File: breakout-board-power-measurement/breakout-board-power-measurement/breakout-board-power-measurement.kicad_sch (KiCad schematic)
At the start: 62 parts, among them J1 Screw_Terminal_01x04, J2 Conn_01x07, J3 Conn_01x07, J4 Conn_01x02, Q1 NMOS, Q2 NMOS, U1 MCP3911A0-E/SS, U2 Si8641BA-B-IU, U3 LM317_3PinPackage, U4 LM2575-3.3BT, Y1 10M

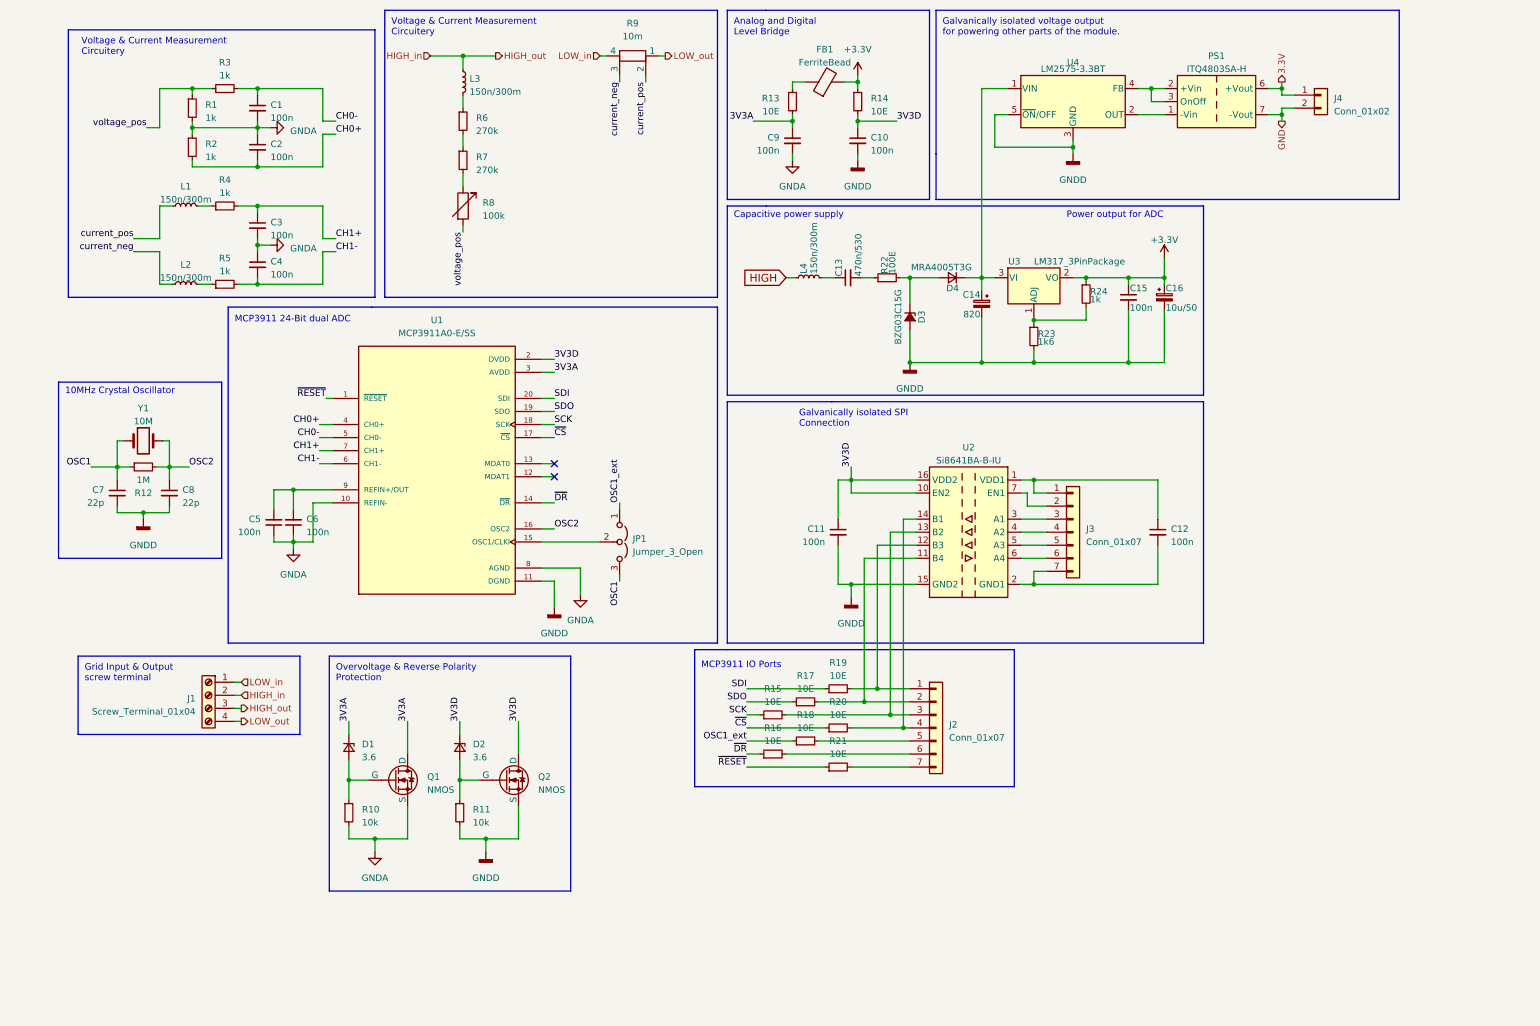
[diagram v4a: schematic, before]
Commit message: Added MCP3911 lib to project specific libraries
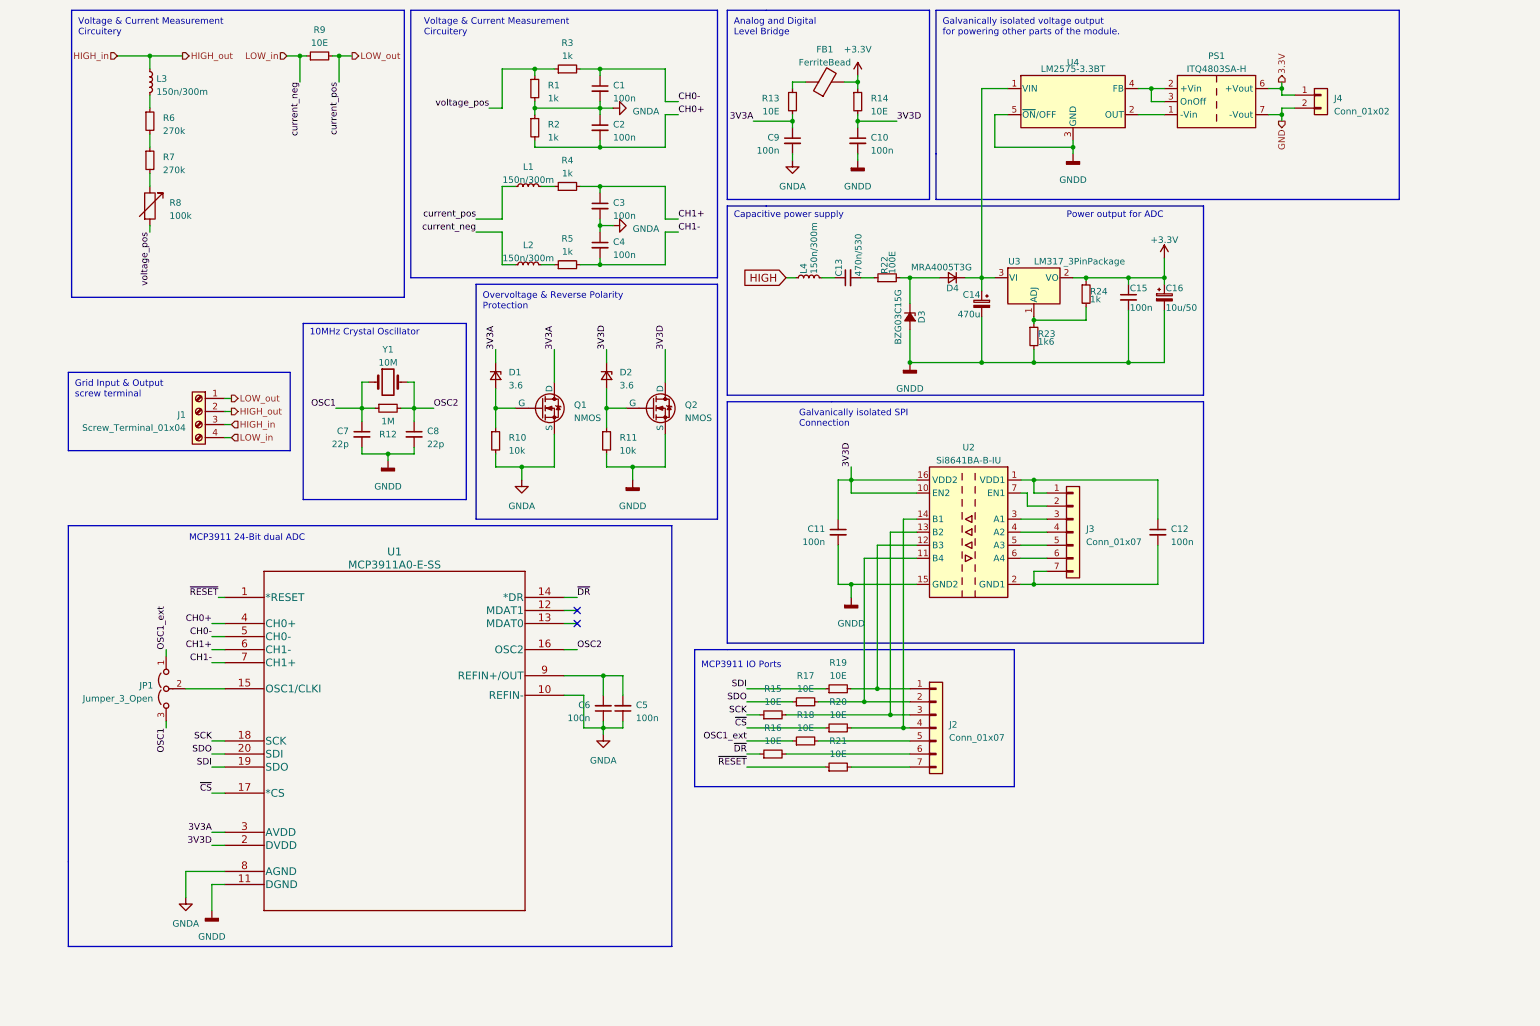
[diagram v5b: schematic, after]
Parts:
- removed R9: 10m, Resistors_THT:R_Axial_DIN0516_L15.5mm_D5.0mm_P20.32mm_Horizontal, symbol Device:R_Shunt
- removed U1: MCP3911A0-E/SS, Housings_SSOP:SSOP-20_5.3x7.2mm_Pitch0.65mm, symbol MCP3911A0-E_SS:MCP3911A0-E/SS
- added R9: 10E, Resistor_SMD:R_2816_7142Metric, symbol Device:R_Small
- added U1: MCP3911A0-E-SS, MCP3911A0-E-SS:MCP3911A0-E&slash_SS, symbol 2023-03-06_20-07-43:MCP3911A0-E/SS
- C13: footprint Capacitors_THT:C_Rect_L26.5mm_W10.5mm_P22.50mm_MKS4 -> Capacitor_THT:C_Rect_L26.5mm_W10.5mm_P22.50mm_MKS4
- C14: value 820 -> 470u; footprint Capacitors_Tantalum_SMD:CP_Tantalum_Case-D_EIA-7343-31_Hand -> Capacitor_Tantalum_SMD:CP_EIA-7343-31_Kemet-D_Pad2.25x2.55mm_HandSolder
- C15: footprint Capacitors_SMD:C_1206_HandSoldering -> Capacitor_SMD:C_1206_3216Metric_Pad1.33x1.80mm_HandSolder
- C16: footprint Capacitors_Tantalum_SMD:CP_Tantalum_Case-D_EIA-7343-31_Hand -> Capacitor_Tantalum_SMD:CP_EIA-7343-31_Kemet-D_Pad2.25x2.55mm_HandSolder
- D1, D2: footprint (none) -> Diode_SMD:D_1206_3216Metric
- D3, D4: footprint Diodes_SMD:D_SMA-SMB_Universal_Handsoldering -> Diode_SMD:D_SMA-SMB_Universal_Handsoldering
- FB1: footprint (none) -> Diode_SMD:D_SMA-SMB_Universal_Handsoldering
- J1: footprint (none) -> TerminalBlock:TerminalBlock_Altech_AK300-4_P5.00mm
- JP1: footprint Pin_Headers:Pin_Header_Straight_1x03_Pitch2.54mm -> Connector_PinHeader_2.54mm:PinHeader_1x03_P2.54mm_Vertical
- L1, L2, L3, L4: footprint Inductors_SMD:L_1206_HandSoldering -> Inductor_SMD:L_1206_3216Metric_Pad1.22x1.90mm_HandSolder
- Q1, Q2: footprint (none) -> Package_TO_SOT_SMD:TO-252-2
- R22, R23, R24: footprint Resistors_SMD:R_1206_HandSoldering -> Resistor_SMD:R_1206_3216Metric_Pad1.30x1.75mm_HandSolder
- R8: footprint Resistor_SMD:R_1206_3216Metric_Pad1.30x1.75mm_HandSolder -> Potentiometer_THT:Potentiometer_ACP_CA9-V10_Vertical_Hole
- U3: footprint TO_SOT_Packages_SMD:SOT-89-3_Handsoldering -> Package_TO_SOT_SMD:SOT-89-3_Handsoldering
- Y1: footprint Crystals:Crystal_HC49-4H_Vertical -> Crystal:Crystal_HC49-4H_Vertical
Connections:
- net current_neg is gone; now on net LOW_in: L2.1
- net current_pos is gone; now on net LOW_out: L1.1
- net 3V3A: now also U1.3 (AVDD)
- net 3V3D: now also U1.2 (DVDD)
- net CH0+: now also U1.4 (CH0+)
- net CH0-: now also U1.5 (CH0-)
- net CH1+: now also U1.6 (CH1-)
- net CH1-: now also U1.7 (CH1+)
- net GNDA: now also U1.10 (REFIN-), U1.8 (AGND)
- net GNDD: now also U1.11 (DGND)
- net LOW_in: now also J1.4 (Pin_4), R9.1; no longer J1.1 (Pin_1)
- net LOW_out: now also J1.1 (Pin_1), R9.2; no longer J1.4 (Pin_4)
- net OSC2: now also U1.16 (OSC2)
- net SCK: now also U1.18 (SCK)
- net SDI: now also U1.19 (SDO)
- net SDO: now also U1.20 (SDI)
- net ~{CS}: now also U1.17 (*CS)
- net ~{DR}: now also U1.14 (*DR)
- net ~{RESET}: now also U1.1 (*RESET)
- net at C5.2, C6.2: now also U1.9 (REFIN+/OUT)
- net at JP1.2 (C): now also U1.15 (OSC1/CLKI)
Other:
- moved on the sheet: C1, C2, C3, C4, C5, C6, C7, C8, D1, D2, J1, JP1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

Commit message: Important updates and fine tunings to schematic
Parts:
- removed D1, D2: 3.6, Diode_SMD:D_1206_3216Metric, symbol Device:D_Zener_Small
- removed PS1: ITQ4803SA-H, Converter_DCDC:Converter_DCDC_XP_POWER-ITQxxxxS-H_THT, symbol Converter_DCDC:ITQ4803SA-H
- removed Q1, Q2: NMOS, Package_TO_SOT_SMD:TO-252-2, symbol Simulation_SPICE:NMOS
- removed U3: LM317_3PinPackage, Package_TO_SOT_SMD:SOT-89-3_Handsoldering, symbol Power-Analyzer-rescue:LM317_3PinPackage
- removed U4: LM2575-3.3BT, Package_TO_SOT_THT:TO-220-5_Vertical, symbol Regulator_Switching:LM2575-3.3BT
- added PS2: IA0505S, Converter_DCDC:Converter_DCDC_XP_POWER-IAxxxxS_THT, symbol Converter_DCDC:IA0505S
- added U3: LM317_TO-252, Package_TO_SOT_SMD:TO-252-2, symbol Regulator_Linear:LM317_TO-252
- J2: value Conn_01x07 -> Conn_01x09; footprint Connector_PinSocket_2.54mm:PinSocket_1x07_P2.54mm_Vertical -> Connector_PinSocket_2.54mm:PinSocket_1x09_P2.54mm_Vertical; symbol Connector_Generic:Conn_01x07 -> Connector_Generic:Conn_01x09
- R10, R11: value 10k -> 180k
- R6, R7: value 270k -> 150k
- R8: value 100k -> 10k
- R9: value 10E -> 50m
- U2: footprint Package_SO:QSOP-16_3.9x4.9mm_P0.635mm -> Package_SO:SOIC-16_3.9x9.9mm_P1.27mm
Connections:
- net +3V3: now also U3.2 (VO)
- net 3.3V: now also PS2.1 (+Vin)
- net 3V3D: now also J2.8 (Pin_8)
- net GND: now also PS2.2 (-Vin)
- net GNDA: no longer R10.2
- net GNDD: now also J2.9 (Pin_9), PS2.4 (-Vout), PS2.5 (0V); no longer R11.2
- net at R10.1: now also R7.2
- net at R11.1: now also R10.2
- net at R8.1: now also R11.2; no longer R7.2
- net at R23.1, R24.2: now also U3.1 (ADJ)
- net at C14.1, D4.1 (K): now also PS2.6 (+Vout), U3.3 (VI)
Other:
- note removed: "Overvoltage & Reverse Polarity Protection"
- moved on the sheet: C1, C10, C11, C12, C13, C14, C15, C16, C2, C3, C4, C5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

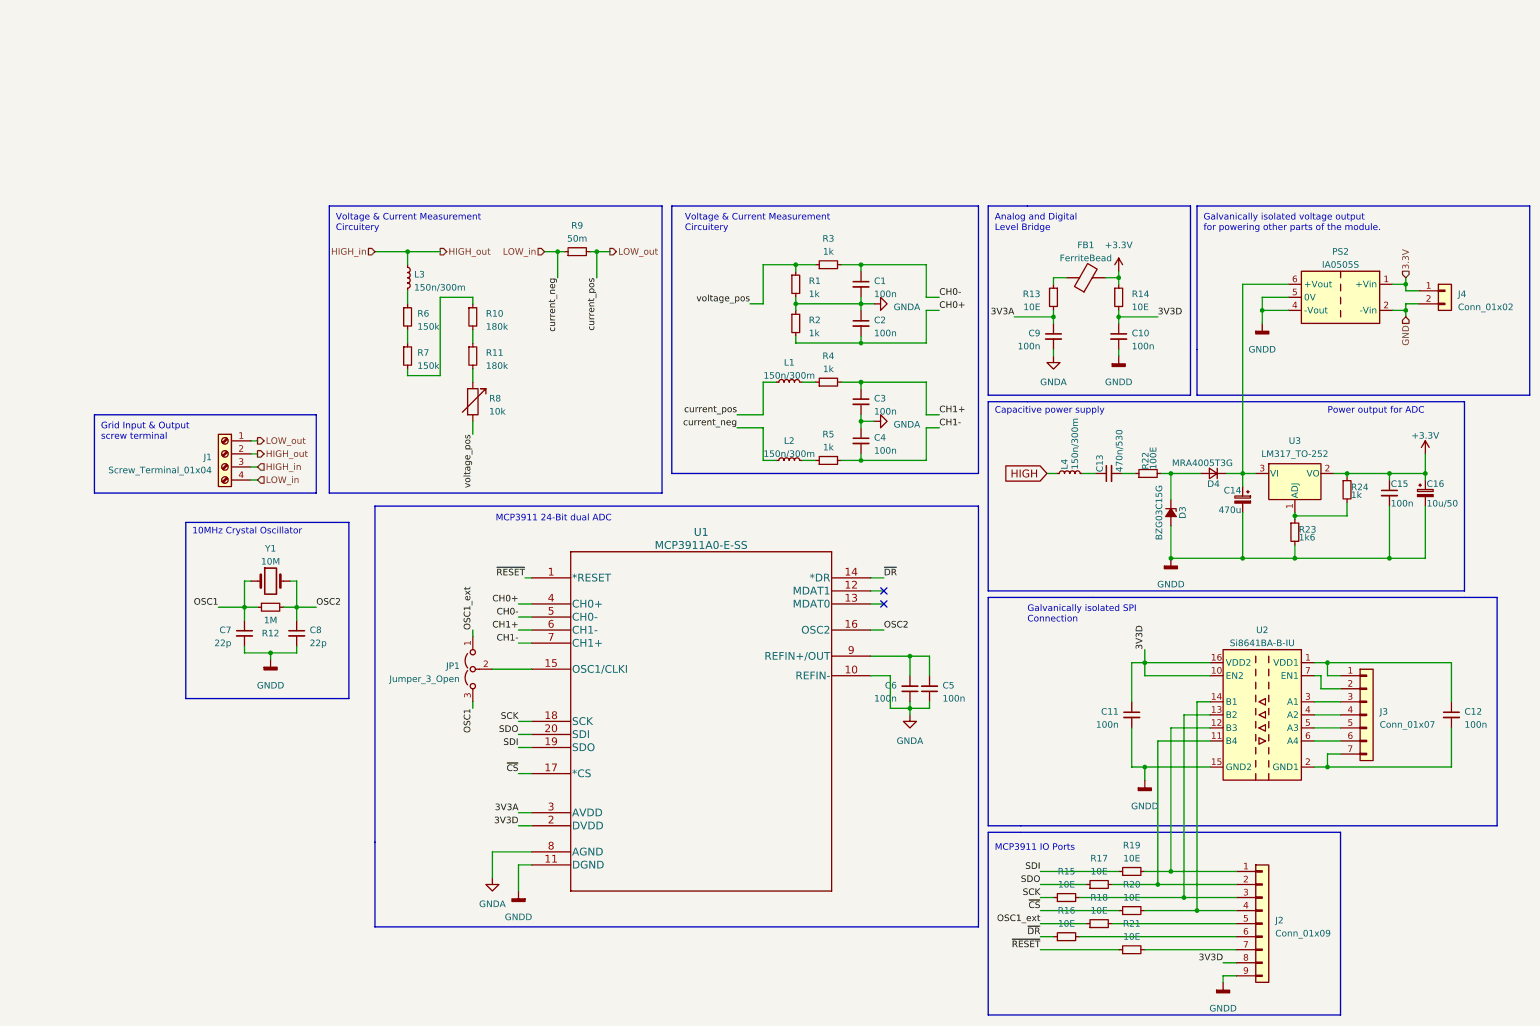
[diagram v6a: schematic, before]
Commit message: Power measurement PCB 95% Done. Whats missing: proper cooil footprints, capacitive power supply net
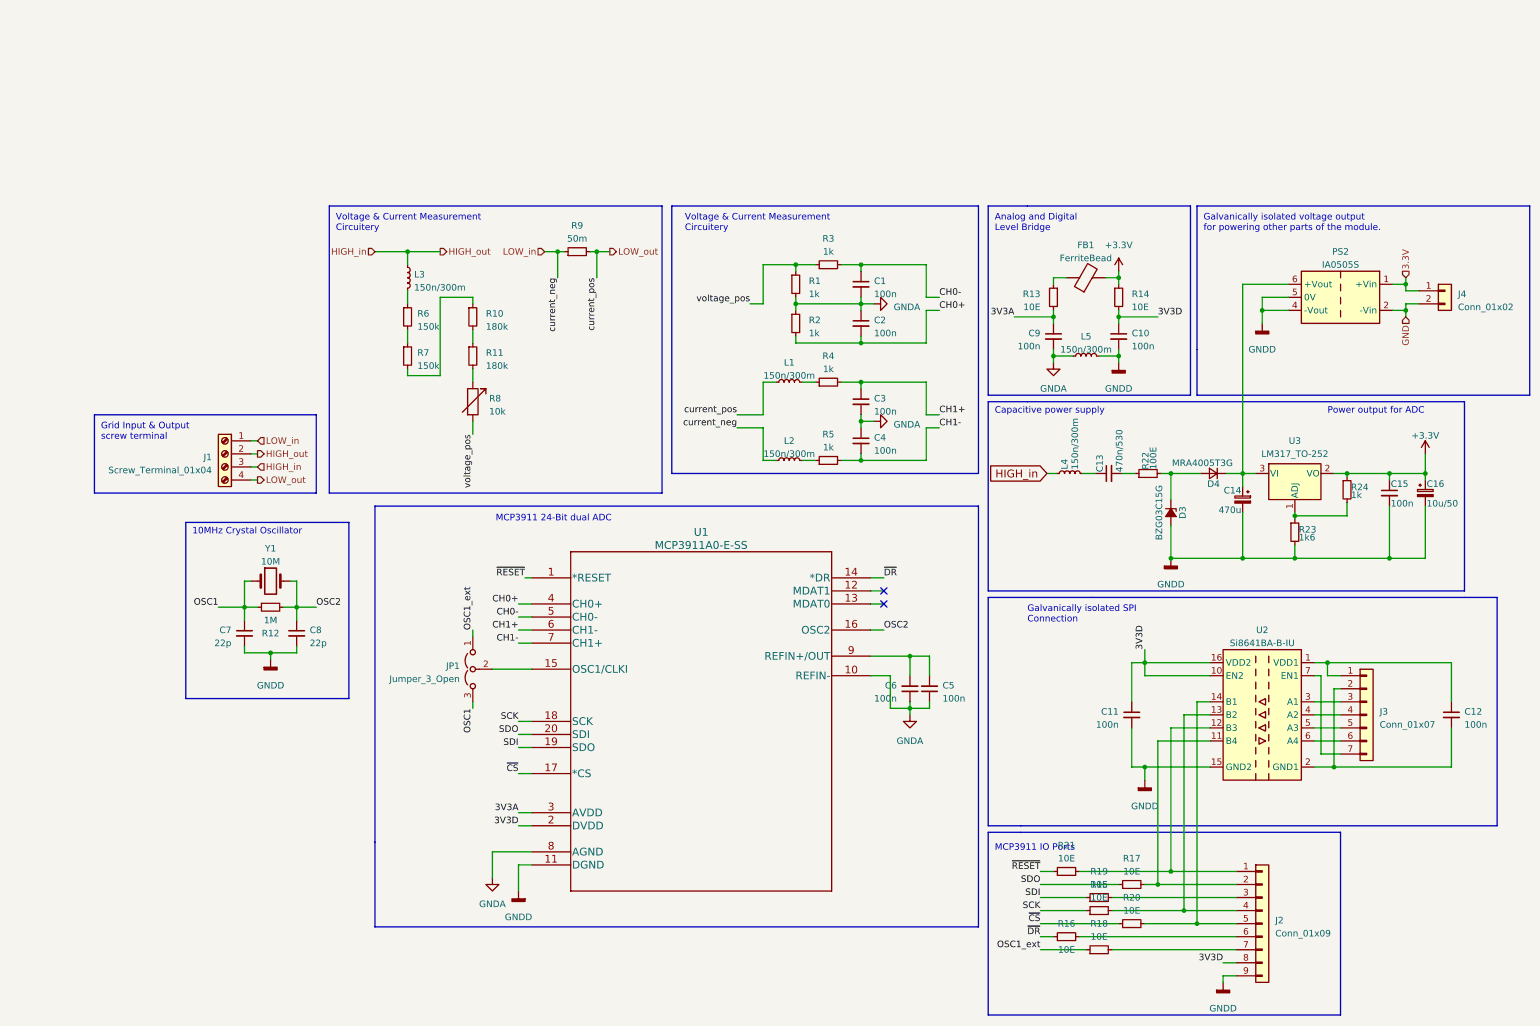
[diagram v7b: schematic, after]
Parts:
- added L5: 150n/300m, Inductor_SMD:L_7.3x7.3_H4.5, symbol Device:L_Small
- L1, L2, L3, L4: footprint Inductor_SMD:L_1206_3216Metric_Pad1.22x1.90mm_HandSolder -> Inductor_SMD:L_7.3x7.3_H4.5
- R9: footprint Resistor_SMD:R_2816_7142Metric -> Resistor_THT:R_Axial_DIN0516_L15.5mm_D5.0mm_P20.32mm_Horizontal
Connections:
- net HIGH is gone; now on net HIGH_in: L4.1
- net GNDA: now also L5.1
- net GNDD: now also L5.2
- net LOW_in: now also J1.1 (Pin_1); no longer J1.4 (Pin_4)
- net LOW_out: now also J1.4 (Pin_4); no longer J1.1 (Pin_1)
- net at J3.2 (Pin_2): now also C12.2, U2.2 (GND1), U2.8 (GND1); no longer U2.7 (EN1)
- net at J2.1 (Pin_1), U2.12 (B3): now also R21.2; no longer R19.2
- net at R15.2, U2.13 (B2): now also J2.4 (Pin_4); no longer J2.3 (Pin_3)
- net at R20.2, U2.14 (B1): now also J2.5 (Pin_5); no longer J2.4 (Pin_4)
- net at R18.2: now also J2.7 (Pin_7); no longer J2.5 (Pin_5)
- new net: J3.7 (Pin_7), U2.7 (EN1)
- new net: J2.3 (Pin_3), R19.2
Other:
- moved on the sheet: R15, R17, R18, R19, R20

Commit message: Breakout Board: Power Measurement - status: done.. yaygit add -A!
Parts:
- added R10, R11, R7, R8: 10m, Resistor_SMD:R_1210_3225Metric, symbol Device:R_Small
- J2: footprint Connector_PinSocket_2.54mm:PinSocket_1x09_P2.54mm_Vertical -> Connector_PinHeader_2.54mm:PinHeader_1x09_P2.54mm_Vertical
- J3: footprint Connector_PinSocket_2.54mm:PinSocket_1x07_P2.54mm_Vertical -> Connector_PinHeader_2.54mm:PinHeader_1x07_P2.54mm_Vertical
- J4: footprint Connector_PinSocket_2.54mm:PinSocket_1x02_P2.54mm_Vertical -> Connector_PinHeader_2.54mm:PinHeader_1x02_P2.54mm_Vertical
- L1: renamed from L3; footprint Inductor_SMD:L_7.3x7.3_H4.5 -> Inductor_SMD:L_1206_3216Metric
- L2: renamed from L1; footprint Inductor_SMD:L_7.3x7.3_H4.5 -> Inductor_SMD:L_1206_3216Metric
- L3: renamed from L2; footprint Inductor_SMD:L_7.3x7.3_H4.5 -> Inductor_SMD:L_1206_3216Metric
- L4, L5: footprint Inductor_SMD:L_7.3x7.3_H4.5 -> Inductor_SMD:L_1206_3216Metric
- R4: renamed from R9; value 50m -> 10m; footprint Resistor_THT:R_Axial_DIN0516_L15.5mm_D5.0mm_P20.32mm_Horizontal -> Resistor_SMD:R_1210_3225Metric
- renumbered C7 to C1, C13 to C10, C10 to C11, C11 to C12, C14 to C13, C15 to C14, C16 to C15, C12 to C16, C8 to C2, C1 to C3, C2 to C4, C3 to C5, C4 to C6, C6 to C7, C5 to C8, D3 to D1, D4 to D2, PS2 to PS1, R12 to R1, R1 to R12, R2 to R13, R3 to R14, R4 to R15, R5 to R16, R13 to R17, R21 to R18, R16 to R19, R6 to R2, R19 to R20, R15 to R21, R18 to R22, R14 to R23, R17 to R24, R20 to R25, R22 to R26, R23 to R27, R24 to R28, R7 to R3, R10 to R5, R11 to R6, R8 to R9
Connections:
- net +3V3 is gone; now on net +3.3V: C14.1, C15.1, R28.1, U3.2 (VO)
- net GNDD: no longer PS1.4 (-Vout)
- net LOW_out: now also R11.2; no longer R4.2
- net 3.3V: no longer names the net of J4.1 (Pin_1), PS1.1 (+Vin)
- net GND: no longer names the net of J4.2 (Pin_2), PS1.2 (-Vin)
- new net: R10.2, R11.1
- new net: R10.1, R8.2
- new net: R7.2, R8.1
- new net: R4.2, R7.1
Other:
- moved on the sheet: R4, R9
